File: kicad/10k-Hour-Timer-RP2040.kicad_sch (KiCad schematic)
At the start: 6 parts, among them J1 USB_C_Receptacle_USB2.0_16P, J2 Conn_01x03_MountingPin, U1 USBLC6-2SC6

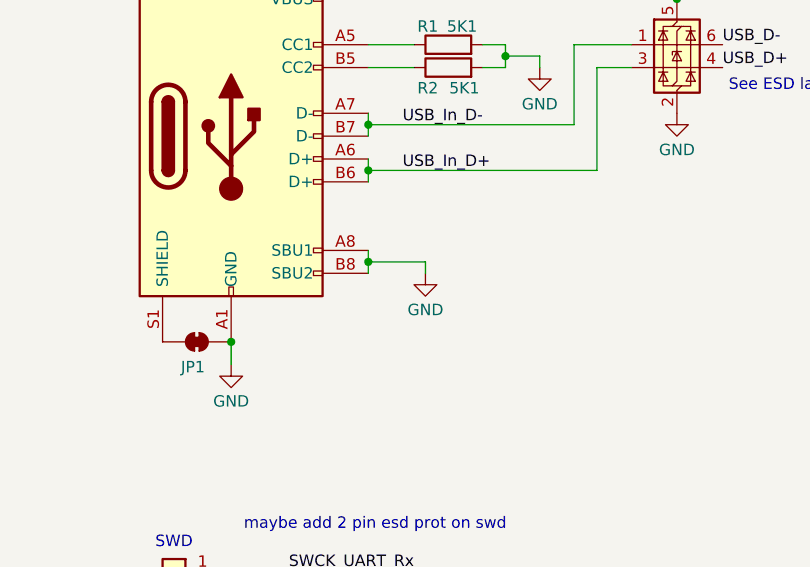
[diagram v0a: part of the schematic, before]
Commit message: 3d model imports
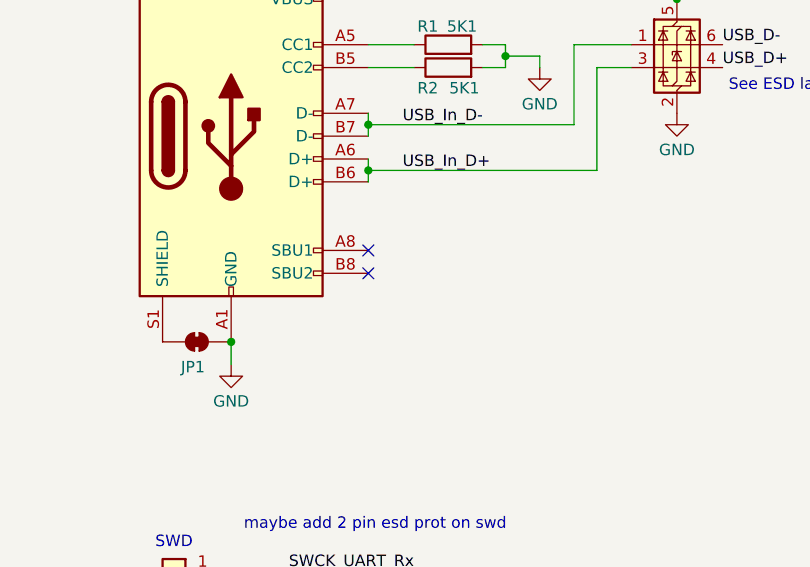
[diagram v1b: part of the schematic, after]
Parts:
- J1: footprint Connector_USB:USB_C_Receptacle_JAE_DX07S016JA1R1500 -> project footprints:USB_C_Receptacle_JAE_DX07S016JA1R1500
- J2: footprint Connector_JST:JST_SH_SM03B-SRSS-TB_1x03-1MP_P1.00mm_Horizontal -> project footprints:JST_SH_SM03B-SRSS-TB_1x03-1MP_P1.00mm_Horizontal
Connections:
- net GND: no longer J1.A8 (SBU1), J1.B8 (SBU2)
- no-connect marks 0 -> 2
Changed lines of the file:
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@@
-	)
-	(junction
-		(at 73.66 86.36)
-		(diameter 0)
-		(color 0 0 0 0)
 	)
 	(junction
@@
 		(color 0 0 0 0)
 	)
+	(no_connect
+		(at 73.66 87.63)
+	)
+	(no_connect
+		(at 73.66 85.09)
+	)
 	(wire
 		(pts
@@
 	(wire
 		(pts
-			(xy 80.01 86.36) (xy 80.01 87.63)
-		)
-		(stroke
-			(width 0)
-			(type default)
-		)
-	)
-	(wire
-		(pts
 			(xy 96.52 62.23) (xy 102.87 62.23)
 		)
@@
 	(wire
 		(pts
-			(xy 73.66 86.36) (xy 73.66 87.63)
-		)
-		(stroke
-			(width 0)
-			(type default)
-		)
-	)
-	(wire
-		(pts
 			(xy 99.06 76.2) (xy 99.06 64.77)
 		)
@@
 	(wire
 		(pts
-			(xy 73.66 86.36) (xy 80.01 86.36)
-		)
-		(stroke
-			(width 0)
-			(type default)
-		)
-	)
-	(wire
-		(pts
 			(xy 73.66 57.15) (xy 107.95 57.15)
 		)
@@
 		(pts
 			(xy 73.66 76.2) (xy 73.66 77.47)
-		)
-		(stroke
-			(width 0)
-			(type default)
-		)
-	)
-	(wire
-		(pts
-			(xy 73.66 85.09) (xy 73.66 86.36)
 		)
 		(stroke
@@
 			)
 		)
-		(property "Footprint" "Connector_JST:JST_SH_SM03B-SRSS-TB_1x03-1MP_P1.00mm_Horizontal"
+		(property "Footprint" "project footprints:JST_SH_SM03B-SRSS-TB_1x03-1MP_P1.00mm_Horizontal"
 			(at 52.07 123.19 0)
 			(effects
@@
 			)
 		)
-		(property "Footprint" "Connector_USB:USB_C_Receptacle_JAE_DX07S016JA1R1500"
+		(property "Footprint" "project footprints:USB_C_Receptacle_JAE_DX07S016JA1R1500"
 			(at 62.23 72.39 0)
 			(effects
@@
 					(unit 1)
 				)
-			)
-		)
-	)
-	(symbol
-		(lib_id "power:GND")
-		(at 80.01 87.63 0)
-		(unit 1)
-		(exclude_from_sim no)
-		(in_bom yes)
-		(on_board yes)
-		(dnp no)
-		(property "Reference" "#PWR04"
-			(at 80.01 93.98 0)
-			(effects
-				(font
-					(size 1.27 1.27)
-				)
-				(hide yes)
-			)
-		)
-		(property "Value" "GND"
-			(at 80.01 91.694 0)
-			(effects
-				(font
-					(size 1.27 1.27)
-				)
-			)
-		)
-		(property "Footprint" ""
-			(at 80.01 87.63 0)
-			(effects
-				(font
-					(size 1.27 1.27)
-				)
-				(hide yes)
-			)
-		)
-		(property "Datasheet" ""
-			(at 80.01 87.63 0)
-			(effects
-				(font
-					(size 1.27 1.27)
-				)
-				(hide yes)
-			)
-		)
-		(property "Description" "Power symbol creates a global label with name \"GND\" , ground"
-			(at 80.01 87.63 0)
-			(effects
-				(font
-					(size 1.27 1.27)
-				)
-				(hide yes)
-			)
-		)
-		(pin "1"
-		)
-		(instances
-			(project "10k-Hour-Timer-RP2040"
-				(path "/9d26b66f-2a94-42e5-8460-016e0bf95186"
-					(reference "#PWR04")
-					(unit 1)
-				)

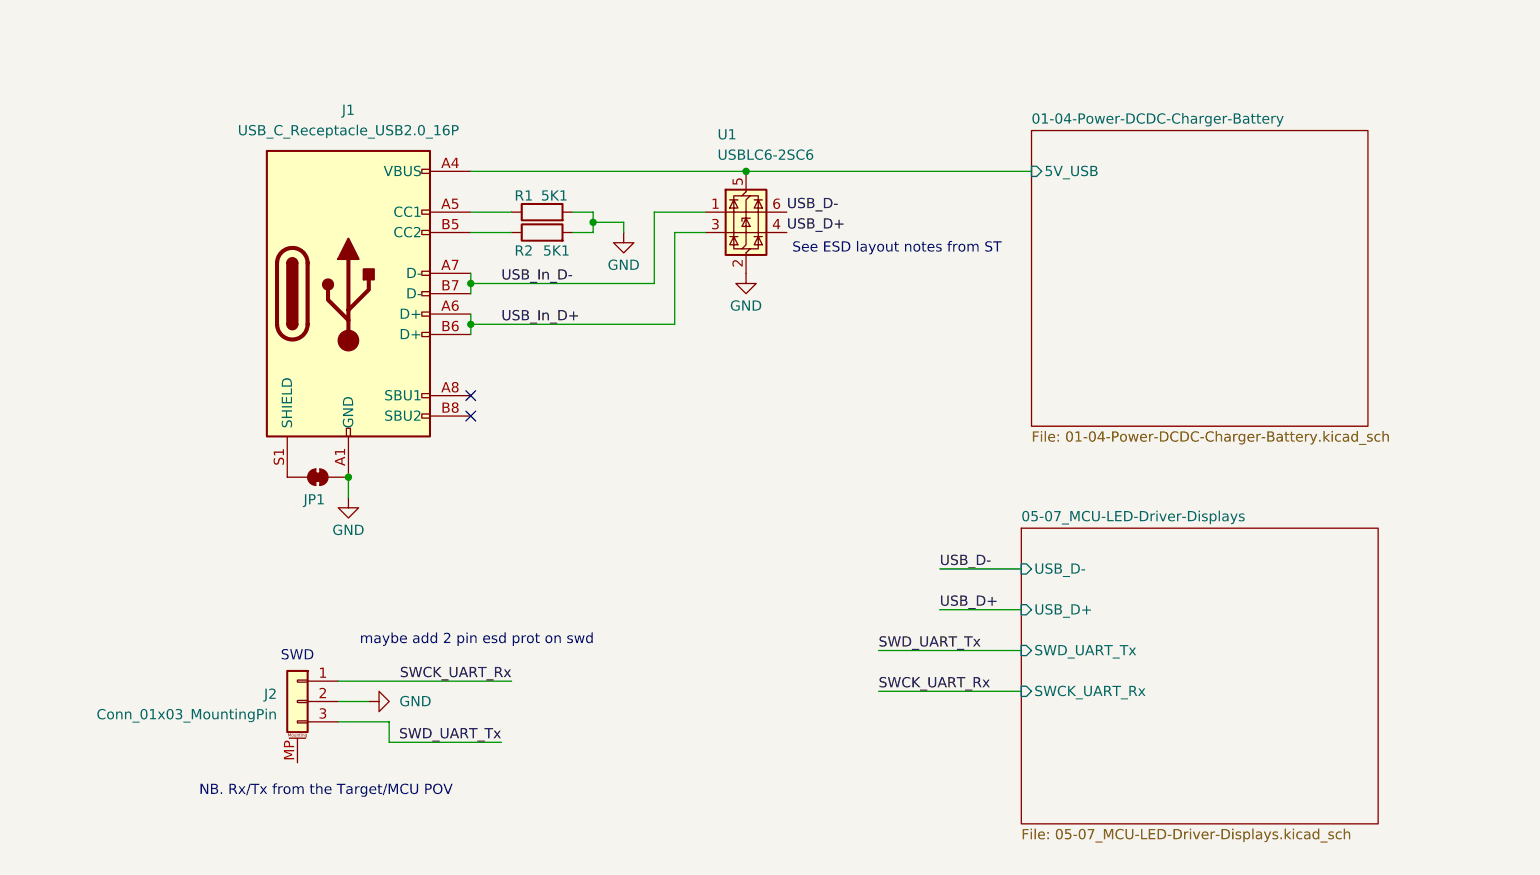
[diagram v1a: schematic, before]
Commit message: added charger and power mux
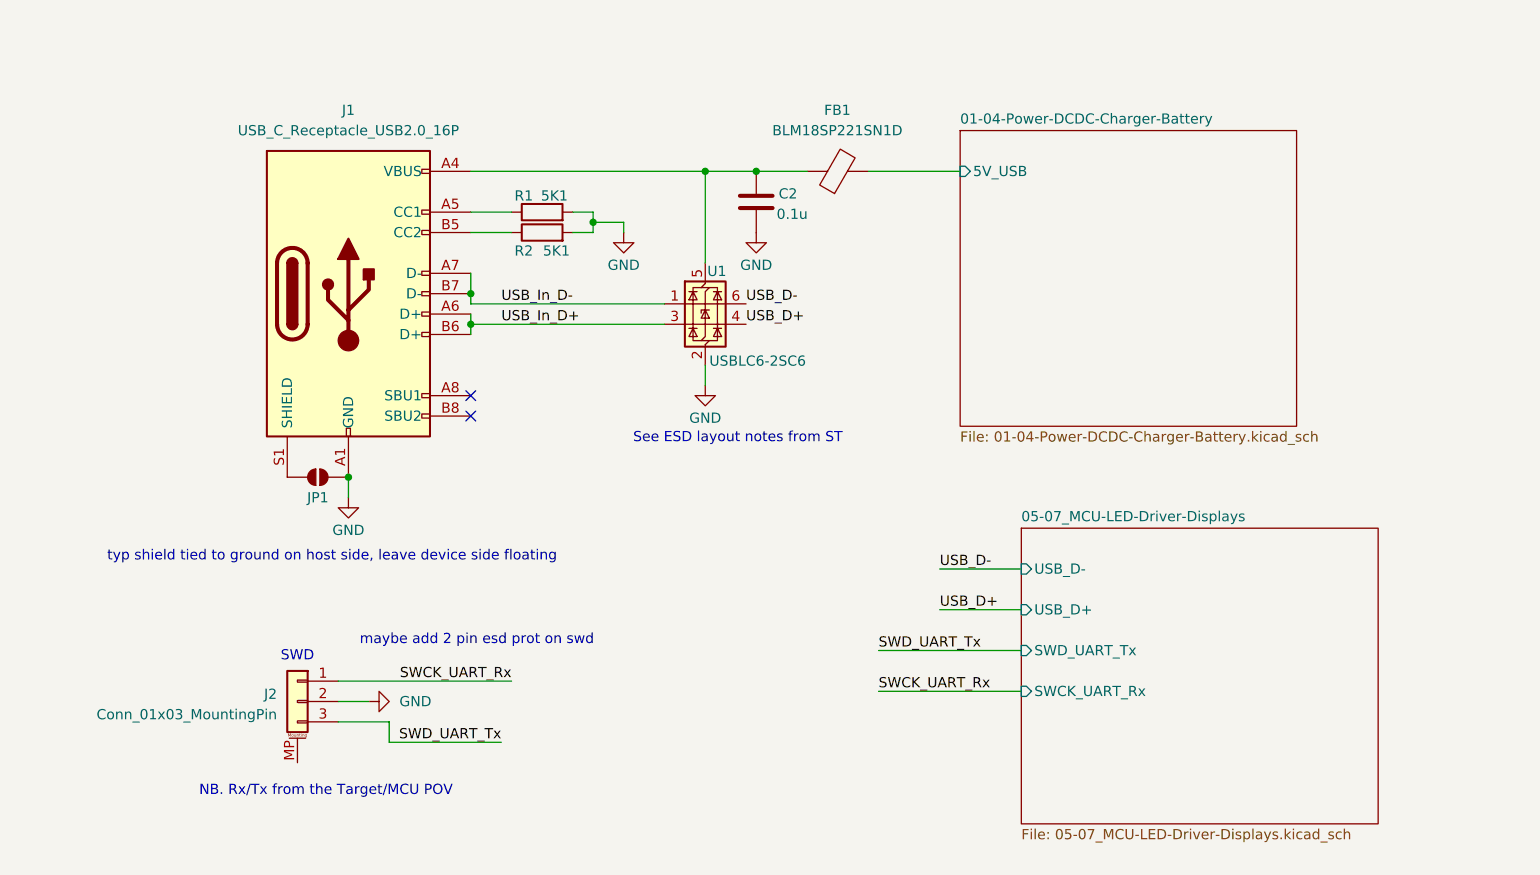
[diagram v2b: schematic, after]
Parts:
- removed JP1: SolderJumper_2_Bridged, symbol Jumper:SolderJumper_2_Bridged
- added C2: 0.1u, symbol Device:C
- added FB1: BLM18SP221SN1D, project footprints:BLM18SP221SN1D_BEADC1608X95N, symbol Device:FerriteBead
- added JP1: SolderJumper_2_Open, symbol Jumper:SolderJumper_2_Open
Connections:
- net 01-04-Power-DCDC-Charger-Battery/5V_USB: now also FB1.2; no longer J1.A4 (VBUS), J1.A9 (VBUS), J1.B4 (VBUS), J1.B9 (VBUS), U1.5 (VBUS)
- net GND: now also C2.2, JP1.2 (B)
- net at J1.S1 (SHIELD): now also JP1.1 (A)
- new net: C2.1, FB1.1, J1.A4 (VBUS), J1.A9 (VBUS), J1.B4 (VBUS), J1.B9 (VBUS), U1.5 (VBUS)
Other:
- note added: "typ shield tied to ground on host side, leave device side floating"
- moved on the sheet: U1

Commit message: dc dc start
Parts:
- added C1: 4u7, symbol Device:C
- J2: value Conn_01x03_MountingPin -> JST_SH_SM03B
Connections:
- net 01-04-Power-DCDC-Charger-Battery/5V_USB: now also C1.1
- net GND: now also J2.MP (MountPin), C1.2
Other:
- sheet 01-04-Power-DCDC-Charger-Battery ports: added BTN_PWR, PWR_CTRL, Vbatt_Vbus; removed none
- sheet 05-07_MCU-LED-Driver-Displays ports: added Vbatt_Vbus; removed none
- note added: "For use with RasPi debugger"

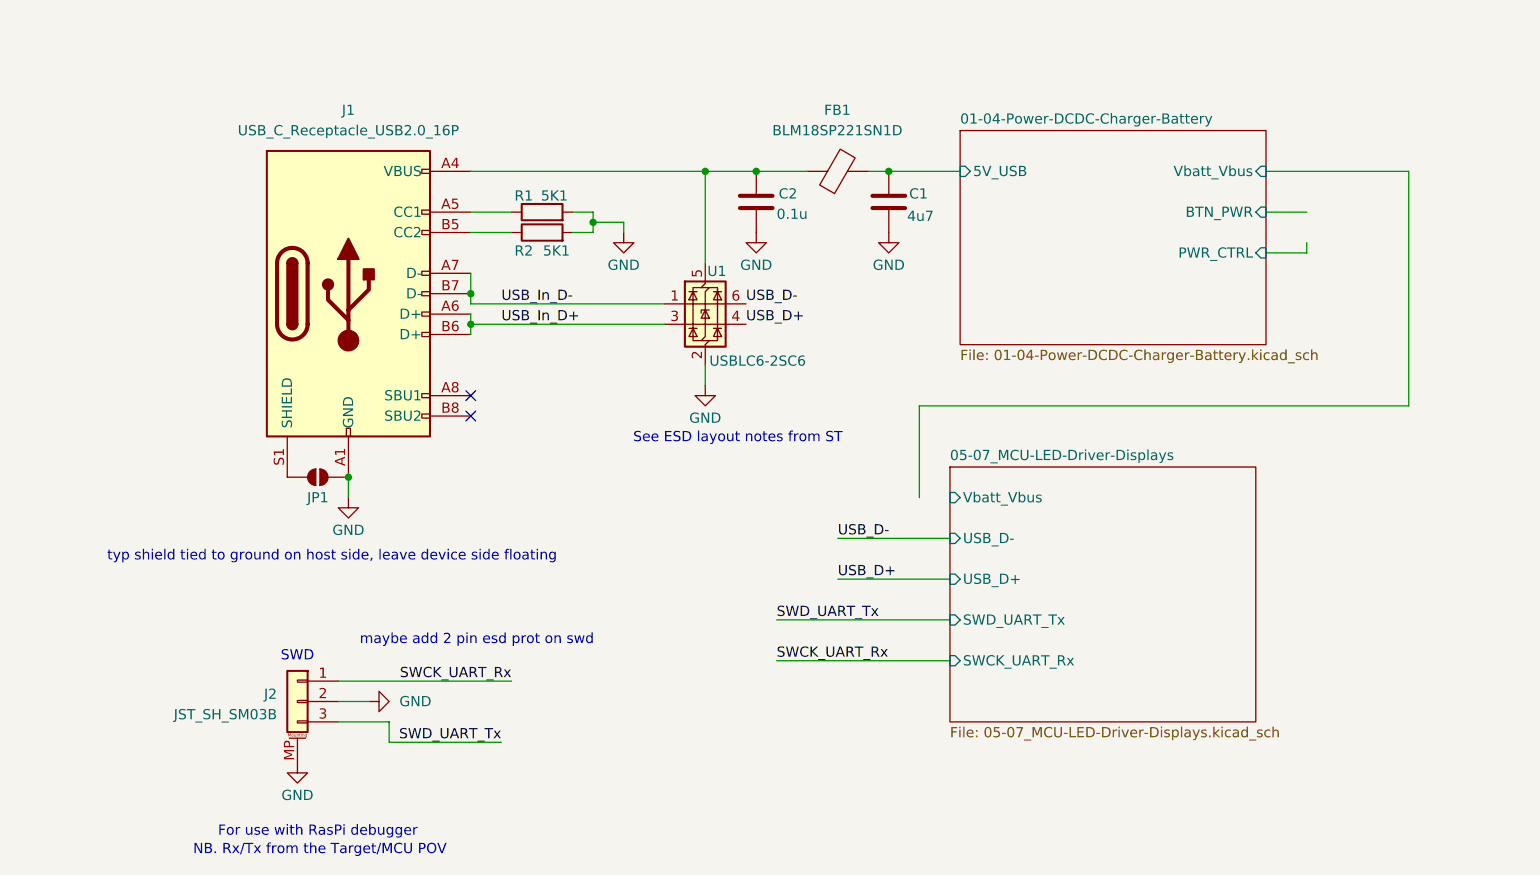
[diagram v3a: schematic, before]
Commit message: dcdc enable and swd
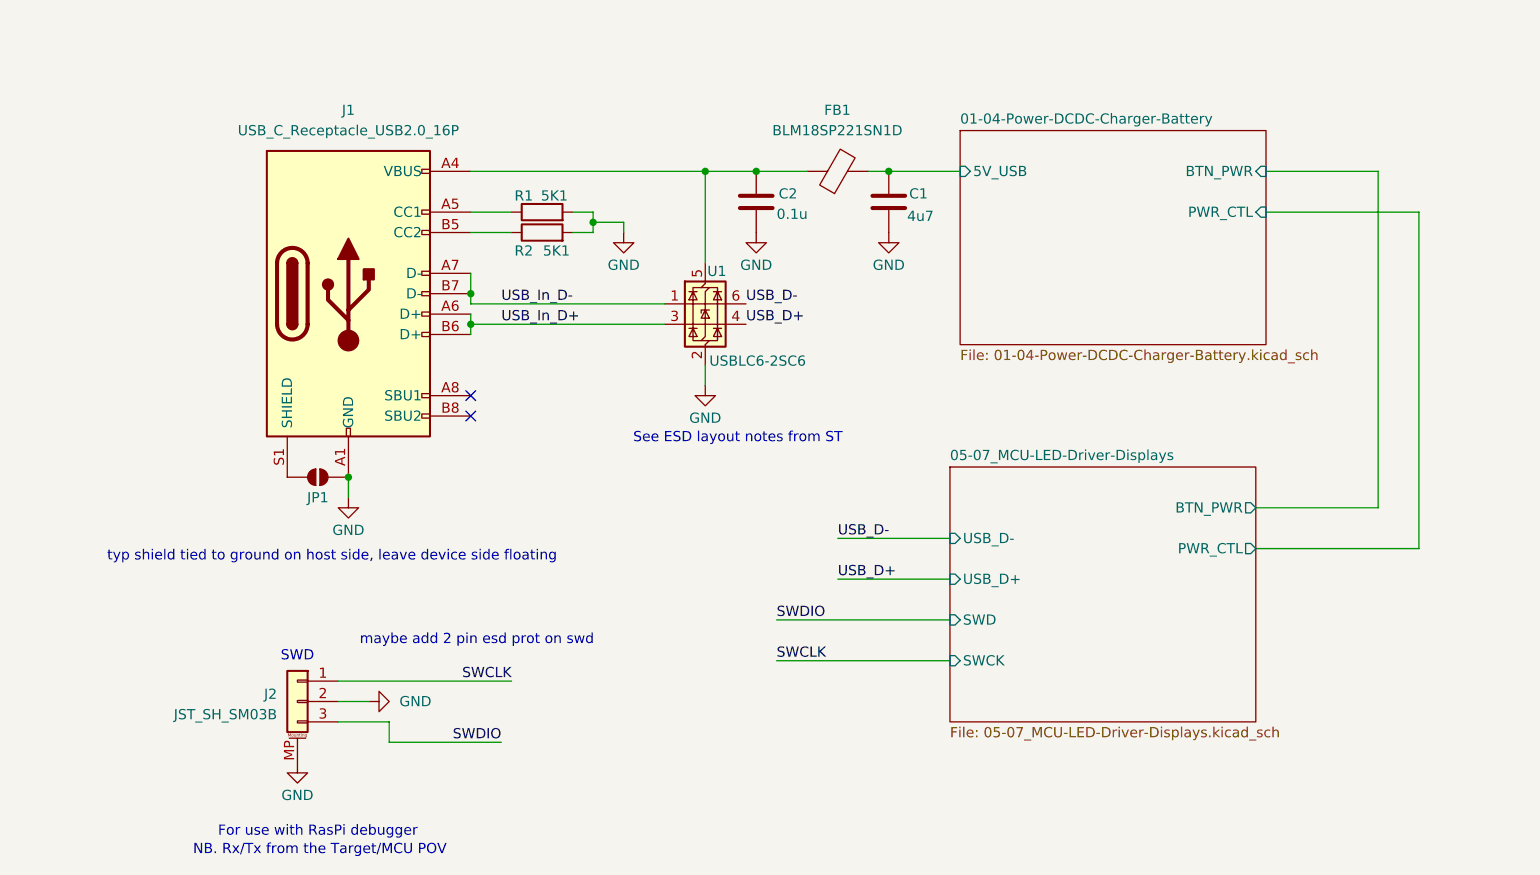
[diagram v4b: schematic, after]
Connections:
- net SWCK_UART_Rx renamed SWCLK
- net SWD_UART_Tx renamed SWDIO
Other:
- sheet 01-04-Power-DCDC-Charger-Battery ports: added PWR_CTL; removed PWR_CTRL, Vbatt_Vbus
- sheet 05-07_MCU-LED-Driver-Displays ports: added BTN_PWR, PWR_CTL, SWCK, SWD; removed SWCK_UART_Rx, SWD_UART_Tx, Vbatt_Vbus
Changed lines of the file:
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@@
+	(wire
+		(pts
+			(xy 186.69 99.06) (xy 186.69 57.15)
+		)
+		(stroke
+			(width 0)
+			(type default)
+		)
+	)
+	(wire
+		(pts
+			(xy 191.77 104.14) (xy 171.45 104.14)
+		)
+		(stroke
+			(width 0)
+			(type default)
+		)
+	)
 	(wire
 		(pts
@@
 	(wire
 		(pts
+			(xy 191.77 62.23) (xy 191.77 104.14)
+		)
+		(stroke
+			(width 0)
+			(type default)
+		)
+	)
+	(wire
+		(pts
 			(xy 102.87 81.28) (xy 102.87 83.82)
 		)
@@
 	(wire
 		(pts
+			(xy 171.45 99.06) (xy 186.69 99.06)
+		)
+		(stroke
+			(width 0)
+			(type default)
+		)
+	)
+	(wire
+		(pts
 			(xy 63.5 128.27) (xy 77.47 128.27)
 		)
@@
 	(wire
 		(pts
-			(xy 172.72 67.31) (xy 177.8 67.31)
+			(xy 172.72 62.23) (xy 191.77 62.23)
 		)
 		(stroke
@@
 	(wire
 		(pts
-			(xy 177.8 66.04) (xy 177.8 67.31)
-		)
-		(stroke
-			(width 0)
-			(type default)
-		)
-	)
-	(wire
-		(pts
-			(xy 190.5 86.36) (xy 129.54 86.36)
-		)
-		(stroke
-			(width 0)
-			(type default)
-		)
-	)
-	(wire
-		(pts
 			(xy 73.66 69.85) (xy 73.66 72.39)
 		)
@@
 	(wire
 		(pts
-			(xy 172.72 57.15) (xy 190.5 57.15)
-		)
-		(stroke
-			(width 0)
-			(type default)
-		)
-	)
-	(wire
-		(pts
 			(xy 111.76 113.03) (xy 133.35 113.03)
 		)
@@
 	(wire
 		(pts
-			(xy 129.54 86.36) (xy 129.54 97.79)
-		)
-		(stroke
-			(width 0)
-			(type default)
-		)
-	)
-	(wire
-		(pts
-			(xy 172.72 62.23) (xy 177.8 62.23)
+			(xy 172.72 57.15) (xy 186.69 57.15)
 		)
 		(stroke
@@
 	(wire
 		(pts
-			(xy 190.5 57.15) (xy 190.5 86.36)
-		)
-		(stroke
-			(width 0)
-			(type default)
-		)
-	)
-	(wire
-		(pts
 			(xy 73.66 73.66) (xy 97.79 73.66)
 		)
@@
 		)
 	)
-	(label "SWCK_UART_Rx"
+	(label "SWCLK"
 		(at 111.76 118.11 0)
 		(effects
@@
 		)
 	)
-	(label "SWCK_UART_Rx"
+	(label "SWCLK"
 		(at 78.74 120.65 180)
 		(effects
@@
 		)
 	)
-	(label "SWD_UART_Tx"
+	(label "SWDIO"
 		(at 111.76 113.03 0)
 		(effects
@@
 		)
 	)
-	(label "SWD_UART_Tx"
+	(label "SWDIO"
 		(at 77.47 128.27 180)
 		(effects
@@
 			)
 		)
-		(pin "SWD_UART_Tx" input
+		(pin "SWD" input
 			(at 133.35 113.03 180)
 			(effects
@@
 			)
 		)
-		(pin "SWCK_UART_Rx" input
+		(pin "SWCK" input
 			(at 133.35 118.11 180)
 			(effects
@@
 			)
 		)
-		(pin "Vbatt_Vbus" input
-			(at 133.35 97.79 180)
-			(effects
-				(font
-					(size 1.27 1.27)
-				)
-				(justify left)
+		(pin "BTN_PWR" output
+			(at 171.45 99.06 0)
+			(effects
+				(font
+					(size 1.27 1.27)
+				)
+				(justify right)
+			)
+		)
+		(pin "PWR_CTL" output
+			(at 171.45 104.14 0)
+			(effects
+				(font
+					(size 1.27 1.27)
+				)
+				(justify right)
 			)
 		)
@@
 			)
 		)
-		(pin "Vbatt_Vbus" input
+		(pin "BTN_PWR" input
 			(at 172.72 57.15 0)
 			(effects
@@
 			)
 		)
-		(pin "BTN_PWR" input
+		(pin "PWR_CTL" input
 			(at 172.72 62.23 0)
 			(effects
 				(font
-					(size 1.27 1.27)
-				)
-				(justify right)
-			)
-		)
-		(pin "PWR_CTRL" input
-			(at 172.72 67.31 0)
-			(effects
-				(font
